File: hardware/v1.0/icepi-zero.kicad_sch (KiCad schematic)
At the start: 25 parts, among them J1 Conn_02x20_Counter_Clockwise, SW1 SW_Push, U1 ECP5U_12_CABGA256

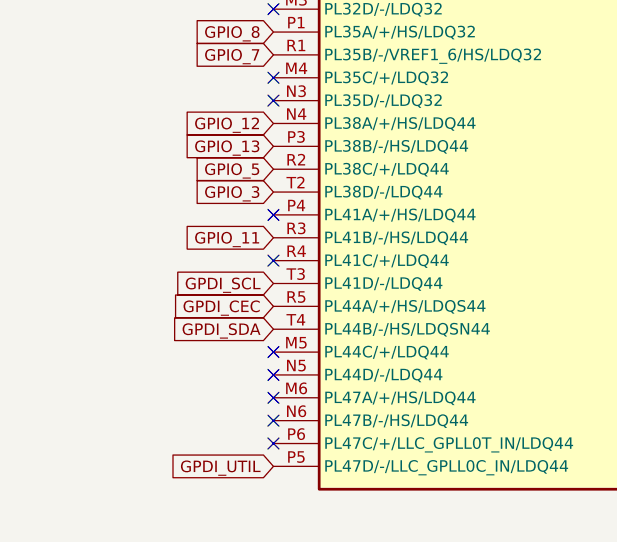
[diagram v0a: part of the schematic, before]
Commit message: Increase pad spacing to 1.9mm and change SCL name to SCK
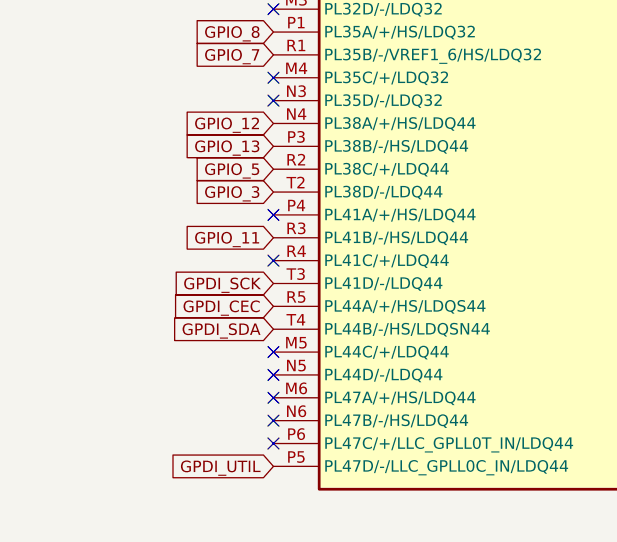
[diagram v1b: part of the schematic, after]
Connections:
- net GPDI_SCL renamed GPDI_SCK
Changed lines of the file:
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@@
 		)
 	)
-	(global_label "GPDI_SCL"
+	(global_label "GPDI_SCK"
 		(shape input)
 		(at 49.53 158.75 180)
